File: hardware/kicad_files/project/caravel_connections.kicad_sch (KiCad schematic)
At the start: 13 parts, among them J10 Conn_01x03_Pin, J7 Conn_01x03_Pin, J8 Conn_01x03_Pin

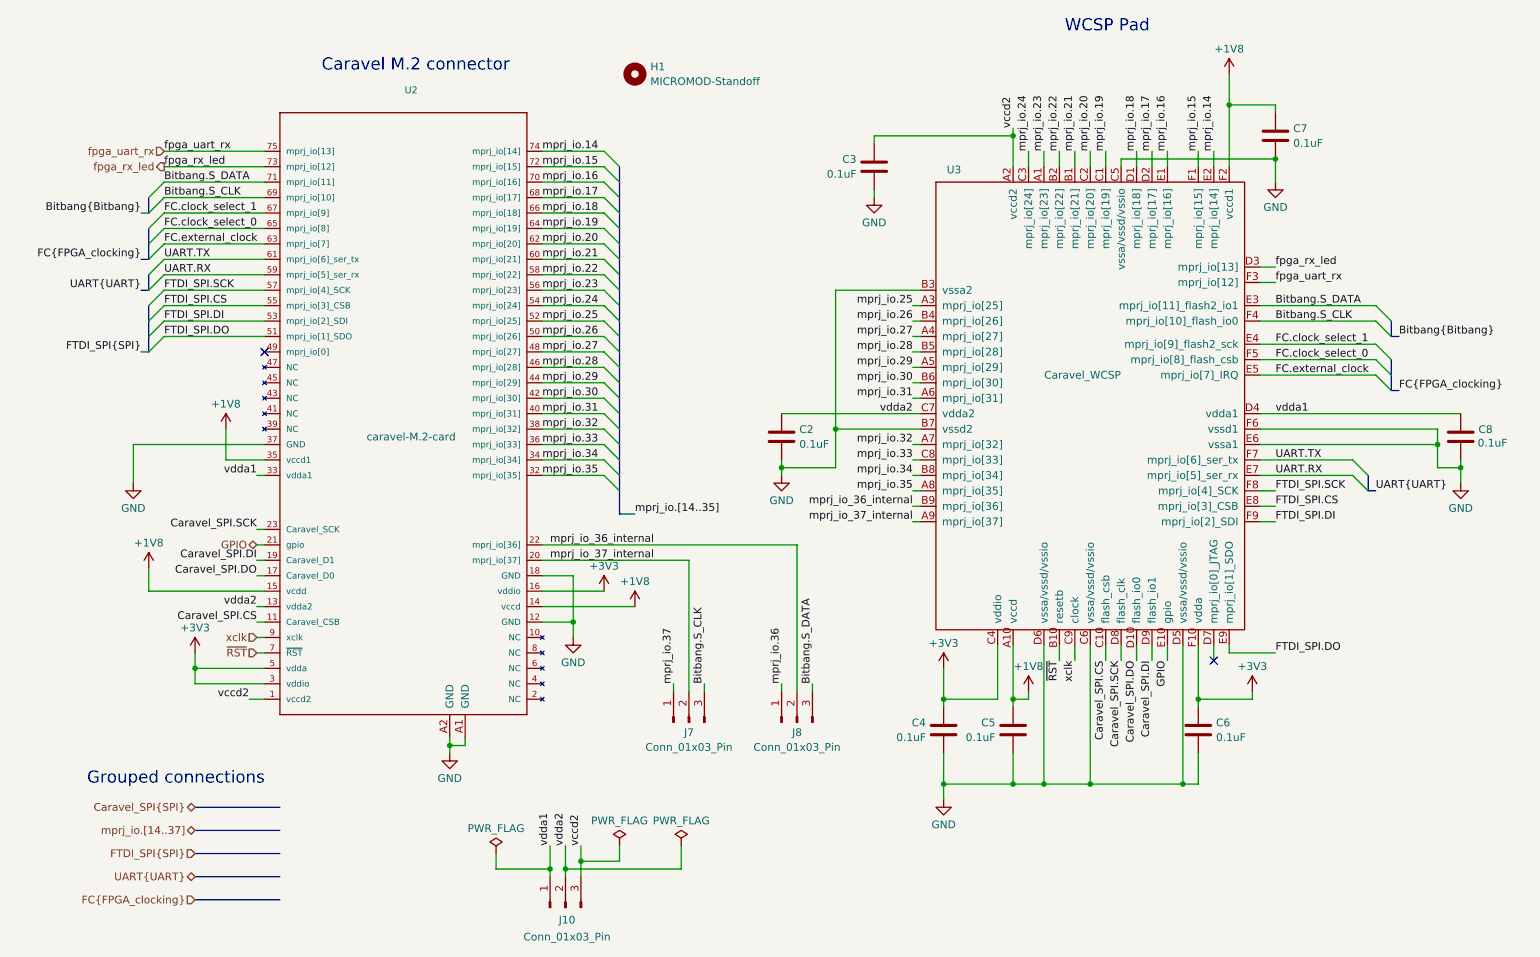
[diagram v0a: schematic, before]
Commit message: feat: optimize layout, reassign annotations, add 2x4 header for UART selection
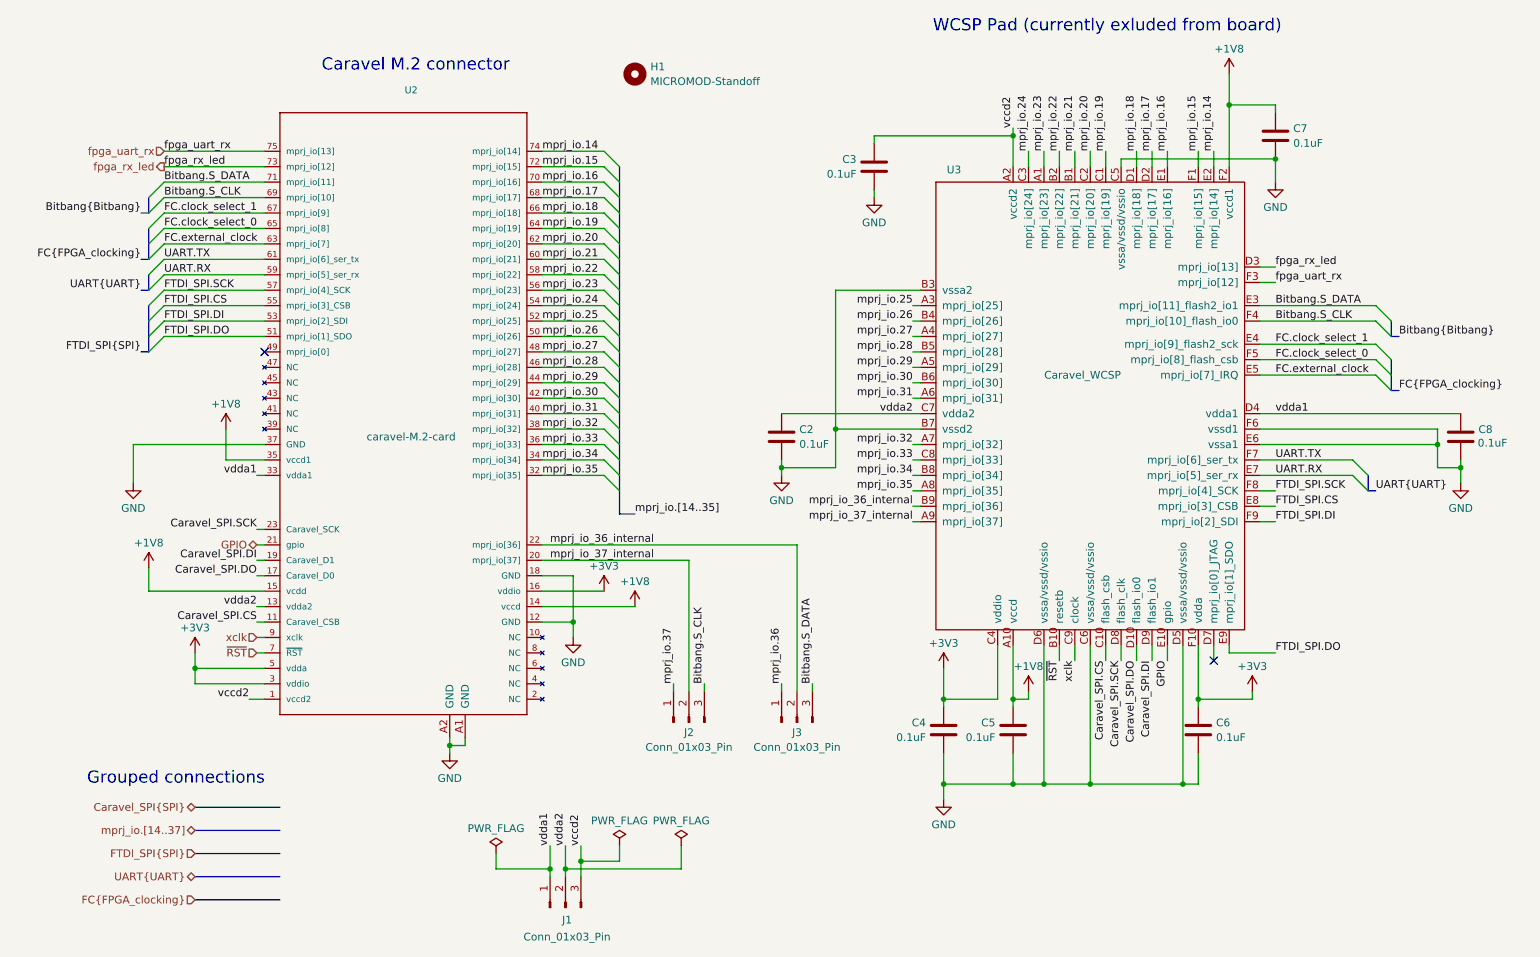
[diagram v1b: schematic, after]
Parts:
- C2, C3, C4, C5, C6, C7, C8, U3: now left out of the parts list
- renumbered J10 to J1, J7 to J2, J8 to J3
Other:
- note added: "WCSP Pad (currently exluded from board)"
- note removed: "WCSP Pad"
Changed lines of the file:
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@@
 		)
 	)
-	(text "WCSP Pad"
+	(text "WCSP Pad (currently exluded from board)"
 		(exclude_from_sim no)
 		(at 208.534 25.146 0)
@@
 		(dnp no)
 		(fields_autoplaced yes)
-		(property "Reference" "#PWR023"
+		(property "Reference" "#PWR024"
 			(at 181.61 158.75 0)
 			(effects
@@
 			(project "FABulous_board"
 				(path "/5664f05e-a3ef-4177-8026-c4580fa32c71/98d779a6-157c-40ed-a845-7459375f17fe"
-					(reference "#PWR023")
+					(reference "#PWR024")
 					(unit 1)
 				)
@@
 		(dnp no)
 		(fields_autoplaced yes)
-		(property "Reference" "#PWR078"
+		(property "Reference" "#PWR014"
 			(at 50.8 118.11 0)
 			(effects
@@
 			(project ""
 				(path "/5664f05e-a3ef-4177-8026-c4580fa32c71/98d779a6-157c-40ed-a845-7459375f17fe"
-					(reference "#PWR078")
+					(reference "#PWR014")
 					(unit 1)
 				)
@@
 		(dnp no)
 		(fields_autoplaced yes)
-		(property "Reference" "#PWR025"
+		(property "Reference" "#PWR029"
 			(at 266.7 106.68 0)
 			(effects
@@
 			(project "FABulous_board"
 				(path "/5664f05e-a3ef-4177-8026-c4580fa32c71/98d779a6-157c-40ed-a845-7459375f17fe"
-					(reference "#PWR025")
+					(reference "#PWR029")
 					(unit 1)
 				)
@@
 		(dnp no)
 		(fields_autoplaced yes)
-		(property "Reference" "#PWR079"
+		(property "Reference" "#PWR025"
 			(at 195.58 138.43 0)
 			(effects
@@
 			(project ""
 				(path "/5664f05e-a3ef-4177-8026-c4580fa32c71/98d779a6-157c-40ed-a845-7459375f17fe"
-					(reference "#PWR079")
+					(reference "#PWR025")
 					(unit 1)
 				)
@@
 		(dnp no)
 		(fields_autoplaced yes)
-		(property "Reference" "#PWR024"
+		(property "Reference" "#PWR028"
 			(at 236.22 57.15 0)
 			(effects
@@
 			(project "FABulous_board"
 				(path "/5664f05e-a3ef-4177-8026-c4580fa32c71/98d779a6-157c-40ed-a845-7459375f17fe"
-					(reference "#PWR024")
+					(reference "#PWR028")
 					(unit 1)
 				)
@@
 		(unit 1)
 		(exclude_from_sim no)
-		(in_bom yes)
-		(on_board yes)
+		(in_bom no)
+		(on_board no)
 		(dnp no)
 		(property "Reference" "C8"
@@
 		(dnp no)
 		(fields_autoplaced yes)
-		(property "Reference" "#PWR016"
+		(property "Reference" "#PWR013"
 			(at 48.26 106.68 0)
 			(effects
@@
 			(project "FABulous_board"
 				(path "/5664f05e-a3ef-4177-8026-c4580fa32c71/98d779a6-157c-40ed-a845-7459375f17fe"
-					(reference "#PWR016")
+					(reference "#PWR013")
 					(unit 1)
 				)
@@
 		(unit 1)
 		(exclude_from_sim no)
-		(in_bom yes)
-		(on_board yes)
+		(in_bom no)
+		(on_board no)
 		(dnp no)
 		(property "Reference" "U3"
@@
 		(dnp no)
 		(fields_autoplaced yes)
-		(property "Reference" "#PWR08"
+		(property "Reference" "#PWR019"
 			(at 125.73 121.92 0)
 			(effects
@@
 			(project ""
 				(path "/5664f05e-a3ef-4177-8026-c4580fa32c71/98d779a6-157c-40ed-a845-7459375f17fe"
-					(reference "#PWR08")
+					(reference "#PWR019")
 					(unit 1)
 				)
@@
 		(dnp no)
 		(fields_autoplaced yes)
-		(property "Reference" "#PWR07"
+		(property "Reference" "#PWR015"
 			(at 58.42 132.08 0)
 			(effects
@@
 			(project ""
 				(path "/5664f05e-a3ef-4177-8026-c4580fa32c71/98d779a6-157c-40ed-a845-7459375f17fe"
-					(reference "#PWR07")
+					(reference "#PWR015")
 					(unit 1)
 				)
@@
 		(dnp no)
 		(fields_autoplaced yes)
-		(property "Reference" "#FLG02"
+		(property "Reference" "#FLG03"
 			(at 138.43 158.115 0)
 			(effects
@@
 			(project "FABulous_board"
 				(path "/5664f05e-a3ef-4177-8026-c4580fa32c71/98d779a6-157c-40ed-a845-7459375f17fe"
-					(reference "#FLG02")
+					(reference "#FLG03")
 					(unit 1)
 				)
@@
 		(unit 1)
 		(exclude_from_sim no)
-		(in_bom yes)
-		(on_board yes)
+		(in_bom no)
+		(on_board no)
 		(dnp no)
 		(property "Reference" "C4"
@@
 		(unit 1)
 		(exclude_from_sim no)
-		(in_bom yes)
-		(on_board yes)
+		(in_bom no)
+		(on_board no)
 		(dnp no)
 		(property "Reference" "C5"
@@
 		(dnp no)
 		(fields_autoplaced yes)
-		(property "Reference" "#PWR082"
+		(property "Reference" "#PWR026"
 			(at 228.6 36.83 0)
 			(effects
@@
 			(project ""
 				(path "/5664f05e-a3ef-4177-8026-c4580fa32c71/98d779a6-157c-40ed-a845-7459375f17fe"
-					(reference "#PWR082")
+					(reference "#PWR026")
 					(unit 1)
 				)
@@
 		(on_board yes)
 		(dnp no)
-		(property "Reference" "J10"
+		(property "Reference" "J1"
 			(at 119.634 172.212 90)
 			(effects
@@
 			(project ""
 				(path "/5664f05e-a3ef-4177-8026-c4580fa32c71/98d779a6-157c-40ed-a845-7459375f17fe"
-					(reference "J10")
+					(reference "J1")
 					(unit 1)
 				)
@@
 		(dnp no)
 		(fields_autoplaced yes)
-		(property "Reference" "#FLG01"
+		(property "Reference" "#FLG02"
 			(at 128.27 158.115 0)
 			(effects
@@
 			(project ""
 				(path "/5664f05e-a3ef-4177-8026-c4580fa32c71/98d779a6-157c-40ed-a845-7459375f17fe"
-					(reference "#FLG01")
+					(reference "#FLG02")
 					(unit 1)
 				)
@@
 		(dnp no)
 		(fields_autoplaced yes)
-		(property "Reference" "#PWR083"
+		(property "Reference" "#PWR027"
 			(at 232.41 138.43 0)
 			(effects
@@
 			(project "FABulous_board"
 				(path "/5664f05e-a3ef-4177-8026-c4580fa32c71/98d779a6-157c-40ed-a845-7459375f17fe"
-					(reference "#PWR083")
+					(reference "#PWR027")
 					(unit 1)
 				)
@@
 		(unit 1)
 		(exclude_from_sim no)
-		(in_bom yes)
-		(on_board yes)
+		(in_bom no)
+		(on_board no)
 		(dnp no)
 		(property "Reference" "C6"
@@
 		(dnp no)
 		(fields_autoplaced yes)
-		(property "Reference" "J7"
+		(property "Reference" "J2"
 			(at 139.7 141.3693 90)
 			(effects
@@
 			(project ""
 				(path "/5664f05e-a3ef-4177-8026-c4580fa32c71/98d779a6-157c-40ed-a845-7459375f17fe"
-					(reference "J7")
+					(reference "J2")
 					(unit 1)
 				)
@@
 		(dnp no)
 		(fields_autoplaced yes)
-		(property "Reference" "J8"
+		(property "Reference" "J3"
 			(at 157.48 141.3693 90)
 			(effects
@@
 			(project "FABulous_board"
 				(path "/5664f05e-a3ef-4177-8026-c4580fa32c71/98d779a6-157c-40ed-a845-7459375f17fe"
-					(reference "J8")
+					(reference "J3")
 					(unit 1)
 				)
@@
 		(unit 1)
 		(exclude_from_sim no)
-		(in_bom yes)
-		(on_board yes)
+		(in_bom no)
+		(on_board no)
 		(dnp no)
 		(property "Reference" "C7"
@@
 		(dnp no)
 		(fields_autoplaced yes)
-		(property "Reference" "#PWR081"
+		(property "Reference" "#PWR016"
 			(at 63.5 95.25 0)
 			(effects
@@
 			(project ""
 				(path "/5664f05e-a3ef-4177-8026-c4580fa32c71/98d779a6-157c-40ed-a845-7459375f17fe"
-					(reference "#PWR081")
+					(reference "#PWR016")
 					(unit 1)
 				)
@@
 		(dnp no)
 		(fields_autoplaced yes)
-		(property "Reference" "#PWR080"
+		(property "Reference" "#PWR023"
 			(at 181.61 134.62 0)
 			(effects
@@
 			(project ""
 				(path "/5664f05e-a3ef-4177-8026-c4580fa32c71/98d779a6-157c-40ed-a845-7459375f17fe"
-					(reference "#PWR080")
+					(reference "#PWR023")
 					(unit 1)
 				)
@@
 		(unit 1)
 		(exclude_from_sim no)
-		(in_bom yes)
-		(on_board yes)
+		(in_bom no)
+		(on_board no)
 		(dnp no)
 		(property "Reference" "C2"
@@
 		(dnp no)
 		(fields_autoplaced yes)
-		(property "Reference" "#FLG03"
+		(property "Reference" "#FLG01"
 			(at 107.95 159.385 0)
 			(effects
@@
 			(project "FABulous_board"
 				(path "/5664f05e-a3ef-4177-8026-c4580fa32c71/98d779a6-157c-40ed-a845-7459375f17fe"
-					(reference "#FLG03")
+					(reference "#FLG01")
 					(unit 1)
 				)
@@
 		(unit 1)
 		(exclude_from_sim no)
-		(in_bom yes)
-		(on_board yes)
+		(in_bom no)
+		(on_board no)
 		(dnp no)
 		(property "Reference" "C3"

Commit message: feat: Implement all findings of the second review
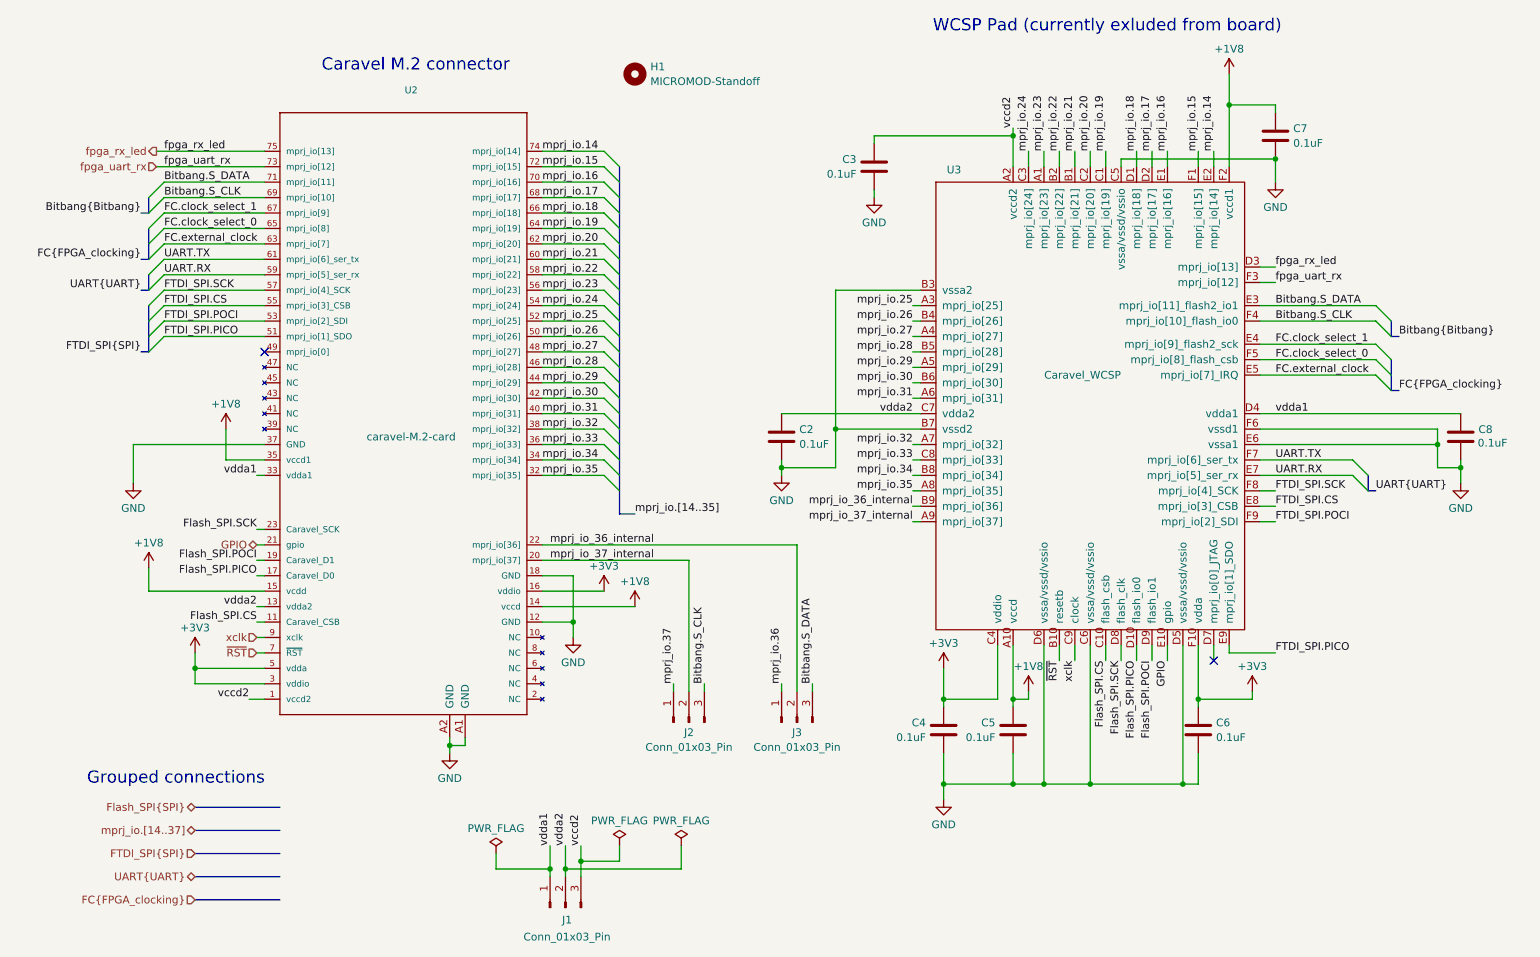
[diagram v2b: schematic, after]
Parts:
- U2: value ~ -> C2977809
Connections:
- net fpga_rx_led: now also U2.75 (mprj_io[13]); no longer U2.73 (mprj_io[12])
- net fpga_uart_rx: now also U2.73 (mprj_io[12]); no longer U2.75 (mprj_io[13])
- net Caravel_SPI.CS renamed Flash_SPI.CS
- net Caravel_SPI.DI renamed Flash_SPI.POCI
- net Caravel_SPI.DO renamed Flash_SPI.PICO
- net Caravel_SPI.SCK renamed Flash_SPI.SCK
- net FTDI_SPI.DI renamed FTDI_SPI.POCI
- net FTDI_SPI.DO renamed FTDI_SPI.PICO
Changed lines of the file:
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@@
 	(wire
 		(pts
-			(xy 53.34 48.26) (xy 69.85 48.26)
-		)
-		(stroke
-			(width 0)
-			(type default)
-		)
-	)
-	(wire
-		(pts
 			(xy 236.22 38.1) (xy 236.22 39.37)
 		)
@@
 	(wire
 		(pts
-			(xy 53.34 45.72) (xy 69.85 45.72)
-		)
-		(stroke
-			(width 0)
-			(type default)
-		)
-	)
-	(wire
-		(pts
 			(xy 233.68 82.55) (xy 252.73 82.55)
 		)
@@
 	(wire
 		(pts
+			(xy 52.07 48.26) (xy 69.85 48.26)
+		)
+		(stroke
+			(width 0)
+			(type default)
+		)
+	)
+	(wire
+		(pts
 			(xy 262.89 91.44) (xy 262.89 93.98)
 		)
@@
 	(wire
 		(pts
+			(xy 52.07 45.72) (xy 69.85 45.72)
+		)
+		(stroke
+			(width 0)
+			(type default)
+		)
+	)
+	(wire
+		(pts
 			(xy 228.6 128.27) (xy 228.6 127)
 		)
@@
 		)
 	)
-	(label "Caravel_SPI.SCK"
+	(label "Flash_SPI.SCK"
 		(at 210.82 129.54 270)
 		(fields_autoplaced yes)
@@
 		)
 	)
-	(label "Caravel_SPI.DI"
+	(label "Flash_SPI.POCI"
 		(at 215.9 129.54 270)
 		(fields_autoplaced yes)
@@
 		)
 	)
-	(label "Caravel_SPI.DO"
+	(label "Flash_SPI.PICO"
 		(at 68.58 115.57 180)
 		(fields_autoplaced yes)
@@
 		)
 	)
-	(label "FTDI_SPI.DO"
+	(label "FTDI_SPI.PICO"
 		(at 236.22 128.27 0)
 		(fields_autoplaced yes)
@@
 		)
 	)
-	(label "FTDI_SPI.DI"
+	(label "FTDI_SPI.POCI"
 		(at 236.22 106.68 0)
 		(fields_autoplaced yes)
@@
 		)
 	)
-	(label "Caravel_SPI.DO"
+	(label "Flash_SPI.PICO"
 		(at 213.36 129.54 270)
 		(fields_autoplaced yes)
@@
 		)
 	)
-	(label "Caravel_SPI.CS"
+	(label "Flash_SPI.CS"
 		(at 208.28 129.54 270)
 		(fields_autoplaced yes)
@@
 	)
 	(label "fpga_uart_rx"
-		(at 53.34 45.72 0)
+		(at 53.34 48.26 0)
 		(fields_autoplaced yes)
 		(effects
@@
 		)
 	)
-	(label "Caravel_SPI.SCK"
+	(label "Flash_SPI.SCK"
 		(at 68.58 107.95 180)
 		(fields_autoplaced yes)
@@
 	)
 	(label "fpga_rx_led"
-		(at 53.34 48.26 0)
+		(at 53.34 45.72 0)
 		(fields_autoplaced yes)
 		(effects
@@
 		)
 	)
-	(label "Caravel_SPI.DI"
+	(label "Flash_SPI.POCI"
 		(at 68.58 113.03 180)
 		(fields_autoplaced yes)
@@
 		)
 	)
-	(label "FTDI_SPI.DI"
+	(label "FTDI_SPI.POCI"
 		(at 53.34 73.66 0)
 		(fields_autoplaced yes)
@@
 		)
 	)
-	(label "FTDI_SPI.DO"
+	(label "FTDI_SPI.PICO"
 		(at 53.34 76.2 0)
 		(fields_autoplaced yes)
@@
 		)
 	)
-	(label "Caravel_SPI.CS"
+	(label "Flash_SPI.CS"
 		(at 68.58 123.19 180)
 		(fields_autoplaced yes)
@@
 		)
 	)
-	(hierarchical_label "Caravel_SPI{SPI}"
+	(hierarchical_label "Flash_SPI{SPI}"
 		(shape bidirectional)
 		(at 58.42 153.67 180)
@@
 	(hierarchical_label "fpga_uart_rx"
 		(shape input)
-		(at 53.34 45.72 180)
+		(at 52.07 48.26 180)
 		(fields_autoplaced yes)
 		(effects
@@
 	(hierarchical_label "fpga_rx_led"
 		(shape output)
-		(at 53.34 48.26 180)
+		(at 52.07 45.72 180)
 		(fields_autoplaced yes)
 		(effects
@@
 			)
 		)
-		(property "Value" "~"
+		(property "Value" "C2977809"
 			(at 93.98 37.879 0)
 			(effects
@@
 					(size 1.143 1.143)
 				)
+				(hide yes)
 			)
 		)

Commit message: fix: add offset for JLCPCB manufacturing
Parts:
- H1: now left out of the parts list
- U2: JLCPCB Position Offset (none) -> 0,-1.45; JLCPCB Rotation Offset (none) -> 180
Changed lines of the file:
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@@
 		(unit 1)
 		(exclude_from_sim no)
-		(in_bom yes)
+		(in_bom no)
 		(on_board yes)
 		(dnp no)
@@
 			)
 		)
+		(property "JLCPCB Position Offset" "0,-1.45"
+			(at 93.98 92.71 0)
+			(effects
+				(font
+					(size 1.27 1.27)
+				)
+				(hide yes)
+			)
+		)
+		(property "JLCPCB Rotation Offset" "180"
+			(at 93.98 92.71 0)
+			(effects
+				(font
+					(size 1.27 1.27)
+				)
+				(hide yes)
+			)
+		)
